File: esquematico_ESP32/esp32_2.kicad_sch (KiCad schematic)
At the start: 9 parts, among them J1 Conn_01x05_Female, SW1 SW_Push, SW2 SW_Push, U1 ESP32-WROOM-32

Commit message: prueba de cambios
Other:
- note added: "potencia"
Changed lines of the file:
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@@
+    (effects (font (size 1.27 1.27)) (justify left bottom))
+  )
+  (text "potencia\n" (at 91.44 130.81 0)
     (effects (font (size 1.27 1.27)) (justify left bottom))
   )

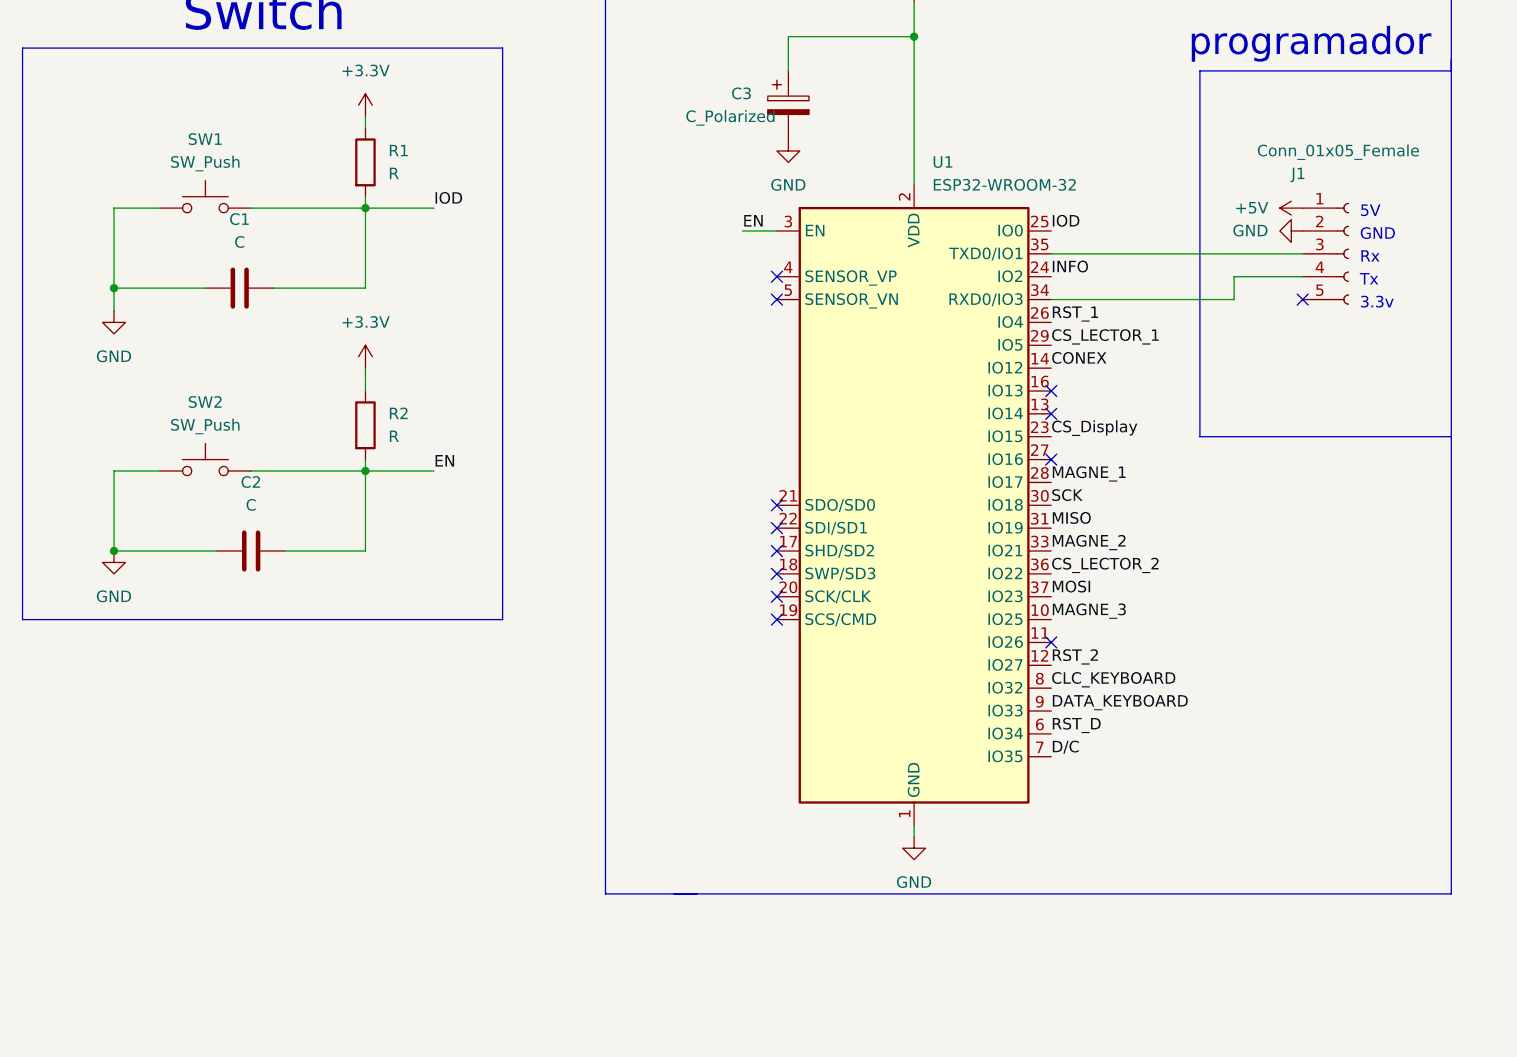
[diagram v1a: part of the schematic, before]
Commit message: ruteo listo con un posible error en footprint esp32
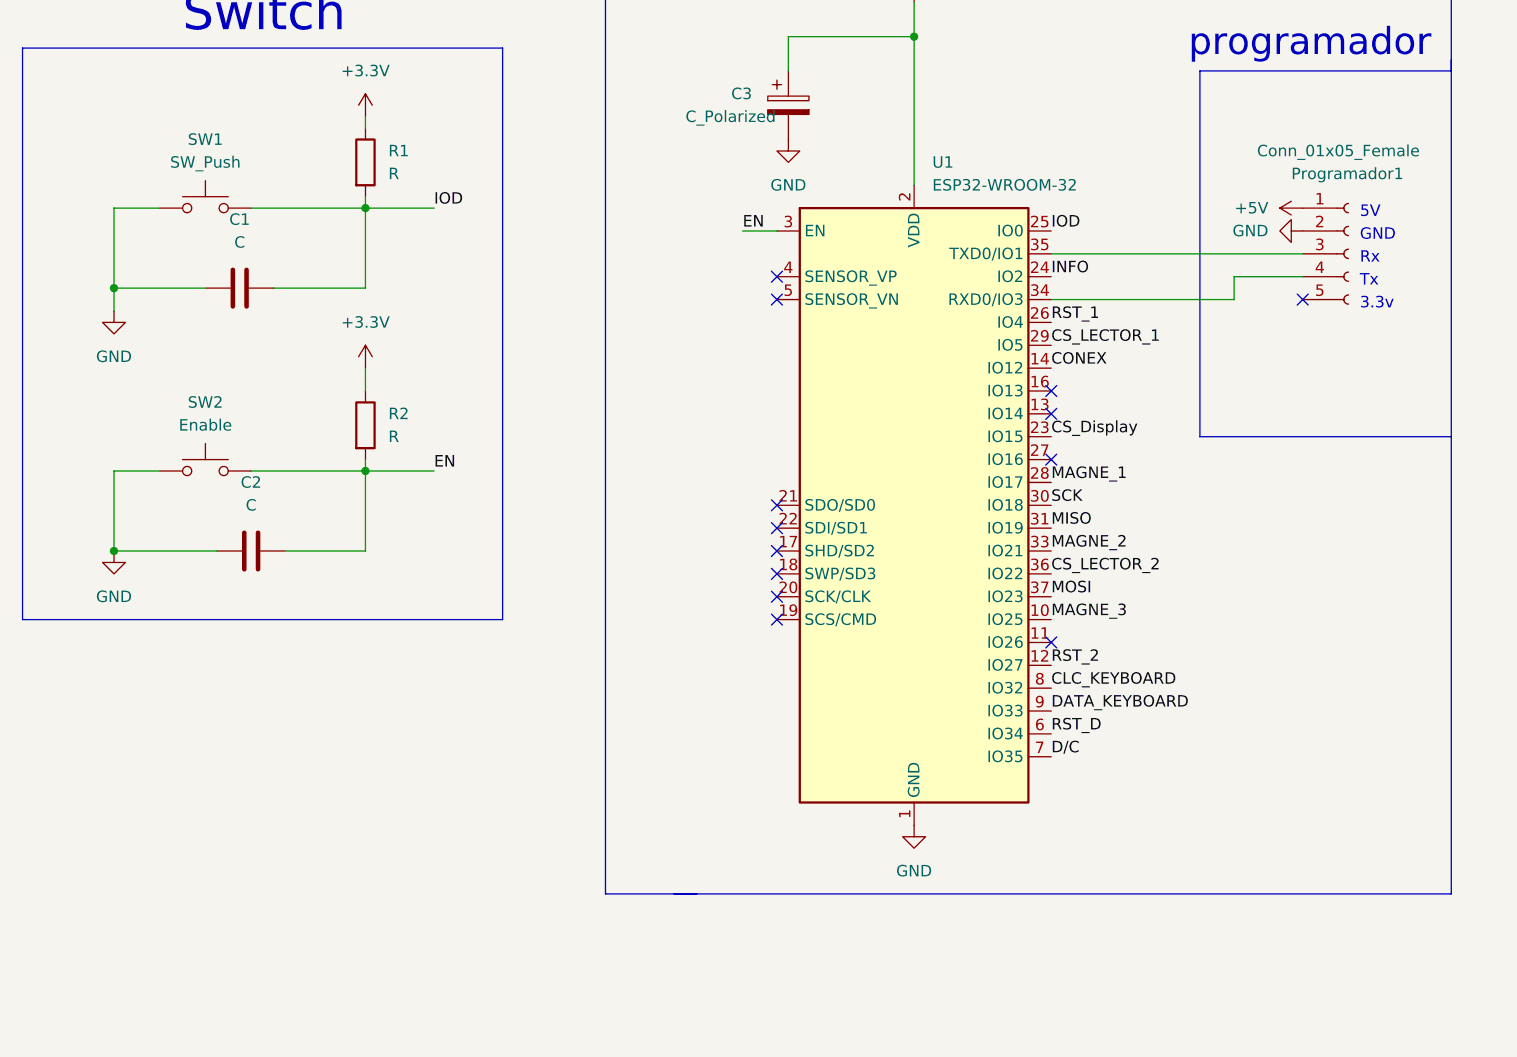
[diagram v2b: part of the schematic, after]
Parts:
- SW2: value SW_Push -> Enable
- renumbered J1 to Programador1
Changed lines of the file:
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@@
-    (stroke (width 0) (type default) (color 0 0 0 0))
-  )
-  (wire (pts (xy 220.98 127) (xy 220.98 125.73))
     (stroke (width 0) (type default) (color 0 0 0 0))
   )
@@
     (pin "1")
   )
-  (symbol (lib_id "power:GND") (at 220.98 127 0) (unit 1)
-    (in_bom yes) (on_board yes) (fields_autoplaced)
-    (property "Reference" "#PWR015" (id 0) (at 220.98 133.35 0)
-      (effects (font (size 1.27 1.27)) hide)
-    )
-    (property "Value" "GND" (id 1) (at 220.98 132.08 0))
-    (property "Footprint" "" (id 2) (at 220.98 127 0)
-      (effects (font (size 1.27 1.27)) hide)
-    )
-    (property "Datasheet" "" (id 3) (at 220.98 127 0)
+  (symbol (lib_id "power:GND") (at 220.98 125.73 0) (unit 1)
+    (in_bom yes) (on_board yes) (fields_autoplaced)
+    (property "Reference" "#PWR015" (id 0) (at 220.98 132.08 0)
+      (effects (font (size 1.27 1.27)) hide)
+    )
+    (property "Value" "GND" (id 1) (at 220.98 130.81 0))
+    (property "Footprint" "" (id 2) (at 220.98 125.73 0)
+      (effects (font (size 1.27 1.27)) hide)
+    )
+    (property "Datasheet" "" (id 3) (at 220.98 125.73 0)
       (effects (font (size 1.27 1.27)) hide)
     )
@@
   (symbol (lib_id "Connector:Conn_01x05_Female") (at 269.24 62.23 0) (unit 1)
     (in_bom yes) (on_board yes)
-    (property "Reference" "J1" (id 0) (at 262.89 53.34 0)
+    (property "Reference" "Programador1" (id 0) (at 262.89 53.34 0)
       (effects (font (size 1.27 1.27)) (justify left))
     )
@@
     (in_bom yes) (on_board yes) (fields_autoplaced)
     (property "Reference" "SW2" (id 0) (at 142.24 78.74 0))
-    (property "Value" "SW_Push" (id 1) (at 142.24 81.28 0))
+    (property "Value" "Enable" (id 1) (at 142.24 81.28 0))
     (property "Footprint" "Button_Switch_SMD:SW_SPST_CK_RS282G05A3" (id 2) (at 142.24 81.28 0)
       (effects (font (size 1.27 1.27)) hide)
@@
       (reference "FB2") (unit 1) (value "FerriteBead") (footprint "Resistor_SMD:R_0603_1608Metric_Pad0.98x0.95mm_HandSolder")
     )
-    (path "/5b1134d1-ab5f-48fa-b527-ffdc1b4c5ff5"
-      (reference "J1") (unit 1) (value "Conn_01x05_Female") (footprint "Connector_PinSocket_2.54mm:PinSocket_1x05_P2.54mm_Horizontal")
-    )
     (path "/90dc18a7-d136-49c5-aca7-9f578dd2dde7/85341b1b-6741-403d-8334-5a36fd82bc82"
-      (reference "J2") (unit 1) (value "Conn_RFID1") (footprint "")
+      (reference "J2") (unit 1) (value "Conn_RFID1") (footprint "Connector_JST:JST_EH_S8B-EH_1x08_P2.50mm_Horizontal")
     )
     (path "/90dc18a7-d136-49c5-aca7-9f578dd2dde7/6f9cf025-6ba5-425e-926b-ef8018e09a41"
-      (reference "J3") (unit 1) (value "Conn_RFID2") (footprint "")
+      (reference "J3") (unit 1) (value "Conn_RFID2") (footprint "Connector_JST:JST_EH_S8B-EH_1x08_P2.50mm_Horizontal")
     )
     (path "/90dc18a7-d136-49c5-aca7-9f578dd2dde7/8229cf0f-f13e-4fa4-b883-d7fe056db563"
@@
     )
     (path "/90dc18a7-d136-49c5-aca7-9f578dd2dde7/879dbbe4-ae64-435d-b735-afdb7f43184d"
-      (reference "J5") (unit 1) (value "Conn_screen") (footprint "")
+      (reference "J5") (unit 1) (value "Conn_screen") (footprint "Connector_JST:JST_EH_S10B-EH_1x10_P2.50mm_Horizontal")
     )
     (path "/90dc18a7-d136-49c5-aca7-9f578dd2dde7/30b53b81-8d67-451d-9f9a-fabac55afe7e"
@@
       (reference "L1") (unit 1) (value "L") (footprint "Inductor_SMD:L_Neosid_SM-PIC0612H")
     )
+    (path "/5b1134d1-ab5f-48fa-b527-ffdc1b4c5ff5"
+      (reference "Programador1") (unit 1) (value "Conn_01x05_Female") (footprint "Connector_PinSocket_2.54mm:PinSocket_1x05_P2.54mm_Horizontal")
+    )
     (path "/90dc18a7-d136-49c5-aca7-9f578dd2dde7/f793cc0c-ede8-43dc-9a01-a81d5ad3f9fc/698ef3e5-c802-45b7-80dd-701416eb8328"
       (reference "Q1") (unit 1) (value "BSS138") (footprint "Package_TO_SOT_SMD:SOT-23")
@@
     )
     (path "/7c72e10d-5c27-41ab-9844-8a388c7b7003"
-      (reference "SW2") (unit 1) (value "SW_Push") (footprint "Button_Switch_SMD:SW_SPST_CK_RS282G05A3")
+      (reference "SW2") (unit 1) (value "Enable") (footprint "Button_Switch_SMD:SW_SPST_CK_RS282G05A3")
     )
     (path "/f73cbebc-ac60-4edc-9956-efadf364e1f4"

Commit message: correción de un pulsador
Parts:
- SW1: footprint Button_Switch_SMD:SW_SPST_EVQQ2 -> Button_Switch_SMD:SW_SPST_CK_RS282G05A3
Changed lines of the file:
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@@
     (property "Reference" "SW1" (id 0) (at 142.24 49.53 0))
     (property "Value" "SW_Push" (id 1) (at 142.24 52.07 0))
-    (property "Footprint" "Button_Switch_SMD:SW_SPST_EVQQ2" (id 2) (at 142.24 52.07 0)
+    (property "Footprint" "Button_Switch_SMD:SW_SPST_CK_RS282G05A3" (id 2) (at 142.24 52.07 0)
       (effects (font (size 1.27 1.27)) hide)
     )
@@
     )
     (path "/68435389-e911-43d9-accd-f38462c79cab"
-      (reference "SW1") (unit 1) (value "SW_Push") (footprint "Button_Switch_SMD:SW_SPST_EVQQ2")
+      (reference "SW1") (unit 1) (value "SW_Push") (footprint "Button_Switch_SMD:SW_SPST_CK_RS282G05A3")
     )
     (path "/7c72e10d-5c27-41ab-9844-8a388c7b7003"
